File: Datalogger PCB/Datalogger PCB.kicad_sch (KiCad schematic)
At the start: 49 parts, among them J1 Conn_01x02_Pin, M1 Motor_Servo, M2 Motor_Servo, M3 Motor_Servo, M4 Motor_Servo, U1 Teensy4.1, U2 BNO055, U3 LPS25HB, U4 AMS1117-5.0, U5 ACPL-214-500E, U6 VN5E160STR-E, U7 VN5E160STR-E, U8 VN5E160STR-E, U9 VN5E160STR-E

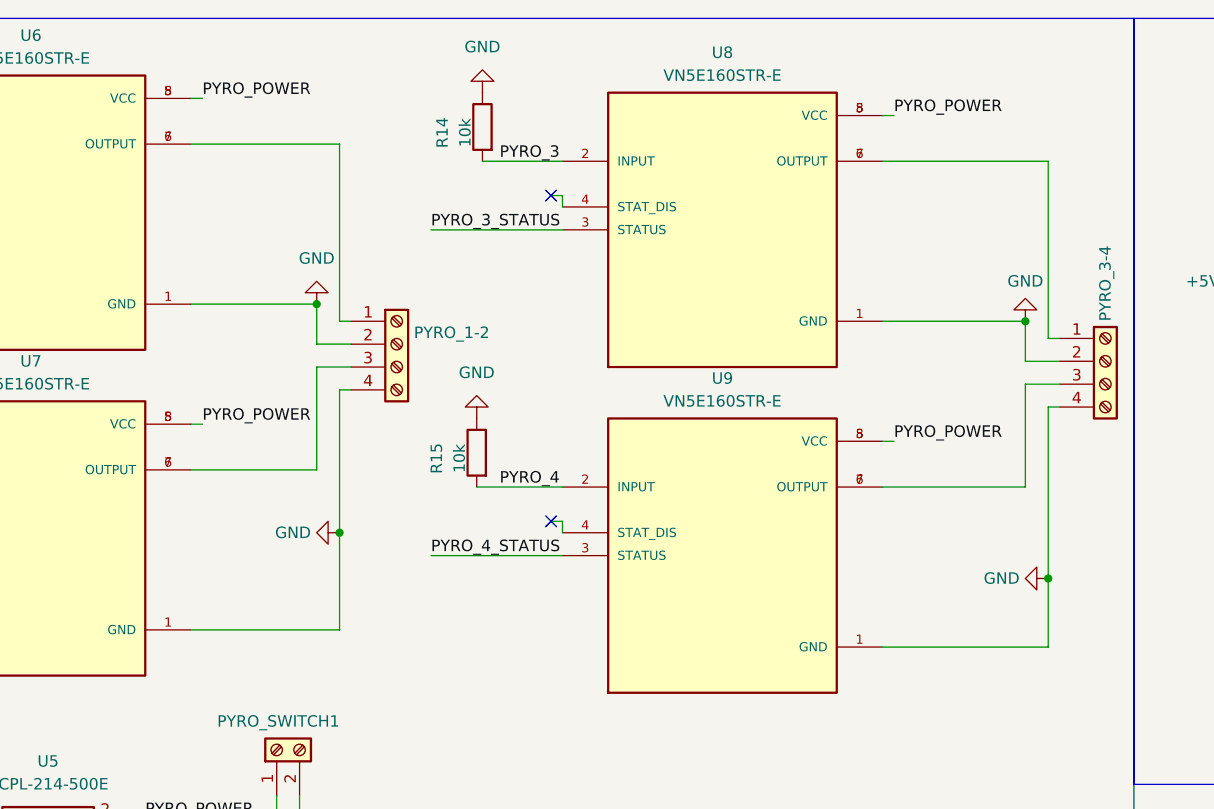
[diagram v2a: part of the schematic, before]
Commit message: Added continuity resistors
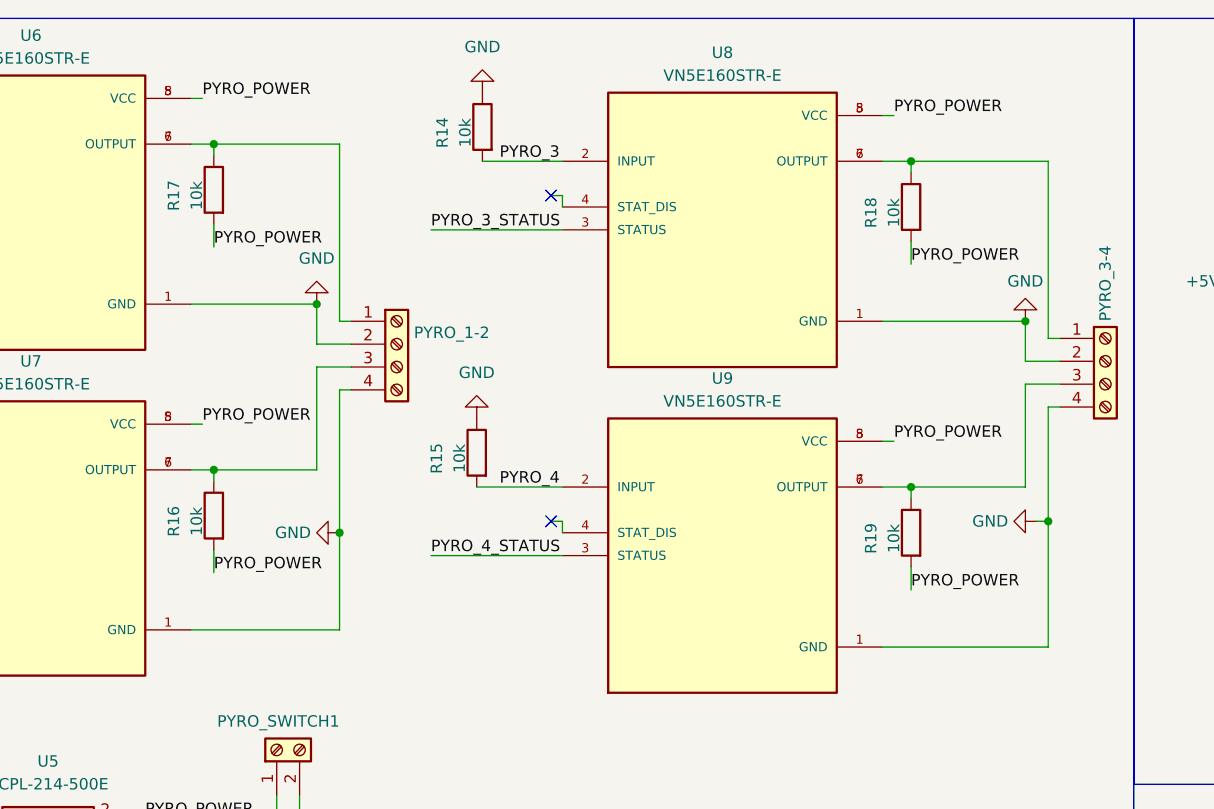
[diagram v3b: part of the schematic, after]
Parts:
- added R16, R17, R18, R19: 10k, Resistor_SMD:R_0603_1608Metric_Pad0.98x0.95mm_HandSolder, symbol Device:R
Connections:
- net PYRO_POWER: now also R16.2, R17.2, R18.2, R19.2
- net at PYRO_3-4.1 (Pin_1), U8.6 (OUTPUT), U8.7 (OUTPUT): now also R18.1
- net at PYRO_3-4.3 (Pin_3), U9.6 (OUTPUT), U9.7 (OUTPUT): now also R19.1
- net at PYRO_1-2.3 (Pin_3), U7.6 (OUTPUT), U7.7 (OUTPUT): now also R16.1
- net at PYRO_1-2.1 (Pin_1), U6.6 (OUTPUT), U6.7 (OUTPUT): now also R17.1

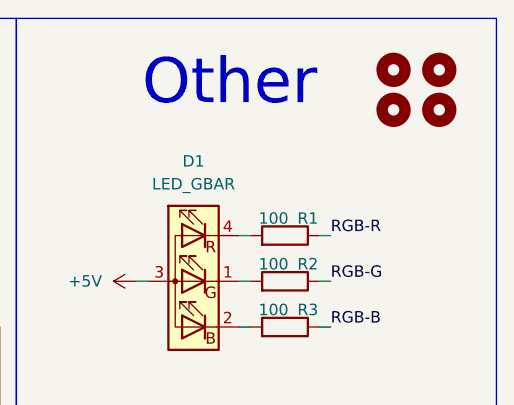
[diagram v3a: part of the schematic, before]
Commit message: Grounded Connector
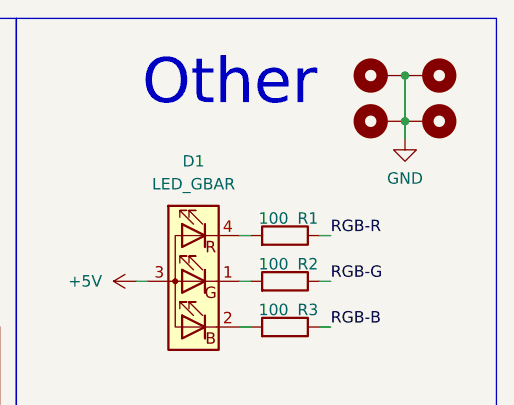
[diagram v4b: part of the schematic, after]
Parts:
- removed H1, H2, H3, H4: MountingHole, MountingHole:MountingHole_3.2mm_M3, symbol Mechanical:MountingHole
- added H1, H2, H3, H4: MountingHole_Pad, MountingHole:MountingHole_3.2mm_M3_Pad_TopBottom, symbol Mechanical:MountingHole_Pad
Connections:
- net GND: now also H1.1, H2.1, H3.1, H4.1
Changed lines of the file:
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@@
   (junction (at 214.63 193.04) (diameter 0) (color 0 0 0 0)
   )
+  (junction (at 333.375 23.495) (diameter 0) (color 0 0 0 0)
+  )
   (junction (at 114.935 155.575) (diameter 0) (color 0 0 0 0)
   )
+  (junction (at 333.375 18.415) (diameter 0) (color 0 0 0 0)
+  )
   (junction (at 280.67 67.945) (diameter 0) (color 0 0 0 0)
   )
@@
     (stroke (width 0) (type default))
   )
+  (wire (pts (xy 333.375 25.4) (xy 333.375 23.495))
+    (stroke (width 0) (type default))
+  )
   (wire (pts (xy 31.75 161.29) (xy 33.02 161.29))
     (stroke (width 0) (type default))
@@
     (stroke (width 0) (type default))
   )
+  (wire (pts (xy 333.375 18.415) (xy 333.375 23.495))
+    (stroke (width 0) (type default))
+  )
   (wire (pts (xy 199.39 164.465) (xy 198.12 164.465))
     (stroke (width 0) (type default))
@@
     (effects (font (size 1.27 1.27)) (justify left bottom))
   )
-  (symbol (lib_id "Mechanical:MountingHole") (at 337.185 22.225 0) (unit 1)
-    (in_bom no) (on_board yes) (dnp no) (fields_autoplaced)
-    (property "Reference" "H4" (at 339.725 20.955 0)
-      (effects (font (size 1.27 1.27)) (justify left) hide)
-    )
-    (property "Value" "MountingHole" (at 339.725 23.495 0)
-      (effects (font (size 1.27 1.27)) (justify left) hide)
-    )
-    (property "Footprint" "MountingHole:MountingHole_3.2mm_M3" (at 337.185 22.225 0)
-      (effects (font (size 1.27 1.27)) hide)
-    )
-    (property "Datasheet" "~" (at 337.185 22.225 0)
-      (effects (font (size 1.27 1.27)) hide)
-    )
-    (instances
-      (project "Datalogger PCB"
-        (path "/a3bc5533-d6ac-45b5-a7d9-fc1b12646794"
-          (reference "H4") (unit 1)
-        )
-      )
-    )
-  )
   (symbol (lib_id "power:GND") (at 182.88 195.58 270) (unit 1)
     (in_bom yes) (on_board yes) (dnp no) (fields_autoplaced)
@@
     )
   )
-  (symbol (lib_id "Mechanical:MountingHole") (at 332.105 17.78 0) (unit 1)
-    (in_bom no) (on_board yes) (dnp no) (fields_autoplaced)
-    (property "Reference" "H1" (at 334.645 16.51 0)
-      (effects (font (size 1.27 1.27)) (justify left) hide)
-    )
-    (property "Value" "MountingHole" (at 334.645 19.05 0)
-      (effects (font (size 1.27 1.27)) (justify left) hide)
-    )
-    (property "Footprint" "MountingHole:MountingHole_3.2mm_M3" (at 332.105 17.78 0)
-      (effects (font (size 1.27 1.27)) hide)
-    )
-    (property "Datasheet" "~" (at 332.105 17.78 0)
-      (effects (font (size 1.27 1.27)) hide)
-    )
-    (instances
-      (project "Datalogger PCB"
-        (path "/a3bc5533-d6ac-45b5-a7d9-fc1b12646794"
-          (reference "H1") (unit 1)
-        )
-      )
-    )
-  )
   (symbol (lib_id "power:+3.3V") (at 199.39 161.925 270) (unit 1)
     (in_bom yes) (on_board yes) (dnp no) (fields_autoplaced)
@@
     )
   )
+  (symbol (lib_id "Mechanical:MountingHole_Pad") (at 335.915 23.495 270) (unit 1)
+    (in_bom yes) (on_board yes) (dnp no)
+    (property "Reference" "H4" (at 338.455 26.67 0)
+      (effects (font (size 1.27 1.27)) (justify left) hide)
+    )
+    (property "Value" "MountingHole_Pad" (at 338.455 27.94 0)
+      (effects (font (size 1.27 1.27)) (justify left) hide)
+    )
+    (property "Footprint" "MountingHole:MountingHole_3.2mm_M3_Pad_TopBottom" (at 335.915 23.495 0)
+      (effects (font (size 1.27 1.27)) hide)
+    )
+    (property "Datasheet" "~" (at 335.915 23.495 0)
+      (effects (font (size 1.27 1.27)) hide)
+    )
+    (pin "1")
+    (instances
+      (project "Datalogger PCB"
+        (path "/a3bc5533-d6ac-45b5-a7d9-fc1b12646794"
+          (reference "H4") (unit 1)
+        )
+      )
+    )
+  )
   (symbol (lib_id "Device:LED_GBAR") (at 309.88 41.275 0) (mirror y) (unit 1)
     (in_bom yes) (on_board yes) (dnp no) (fields_autoplaced)
@@
     )
   )
+  (symbol (lib_id "power:GND") (at 333.375 25.4 0) (unit 1)
+    (in_bom yes) (on_board yes) (dnp no) (fields_autoplaced)
+    (property "Reference" "#PWR036" (at 333.375 31.75 0)
+      (effects (font (size 1.27 1.27)) hide)
+    )
+    (property "Value" "GND" (at 333.375 29.845 0)
+      (effects (font (size 1.27 1.27)))
+    )
+    (property "Footprint" "" (at 333.375 25.4 0)
+      (effects (font (size 1.27 1.27)) hide)
+    )
+    (property "Datasheet" "" (at 333.375 25.4 0)
+      (effects (font (size 1.27 1.27)) hide)
+    )
+    (pin "1")
+    (instances
+      (project "Datalogger PCB"
+        (path "/a3bc5533-d6ac-45b5-a7d9-fc1b12646794"
+          (reference "#PWR036") (unit 1)
+        )
+      )
+    )
+  )
   (symbol (lib_id "Device:C") (at 109.855 158.75 270) (mirror x) (unit 1)
     (in_bom yes) (on_board yes) (dnp no)
@@
     )
   )
+  (symbol (lib_id "Mechanical:MountingHole_Pad") (at 330.835 18.415 90) (unit 1)
+    (in_bom yes) (on_board yes) (dnp no)
+    (property "Reference" "H1" (at 328.295 15.24 0)
+      (effects (font (size 1.27 1.27)) (justify left) hide)
+    )
+    (property "Value" "MountingHole_Pad" (at 328.295 13.97 0)
+      (effects (font (size 1.27 1.27)) (justify left) hide)
+    )
+    (property "Footprint" "MountingHole:MountingHole_3.2mm_M3_Pad_TopBottom" (at 330.835 18.415 0)
+      (effects (font (size 1.27 1.27)) hide)
+    )
+    (property "Datasheet" "~" (at 330.835 18.415 0)
+      (effects (font (size 1.27 1.27)) hide)
+    )
+    (pin "1")
+    (instances
+      (project "Datalogger PCB"
+        (path "/a3bc5533-d6ac-45b5-a7d9-fc1b12646794"
+          (reference "H1") (unit 1)
+        )
+      )
+    )
+  )
   (symbol (lib_id "power:GND") (at 308.61 63.5 270) (mirror x) (unit 1)
     (in_bom yes) (on_board yes) (dnp no) (fields_autoplaced)
@@
     )
   )
-  (symbol (lib_id "Mechanical:MountingHole") (at 332.105 22.225 0) (unit 1)
-    (in_bom no) (on_board yes) (dnp no) (fields_autoplaced)
-    (property "Reference" "H3" (at 334.645 20.955 0)
-      (effects (font (size 1.27 1.27)) (justify left) hide)
-    )
-    (property "Value" "MountingHole" (at 334.645 23.495 0)
-      (effects (font (size 1.27 1.27)) (justify left) hide)
-    )
-    (property "Footprint" "MountingHole:MountingHole_3.2mm_M3" (at 332.105 22.225 0)
-      (effects (font (size 1.27 1.27)) hide)
-    )
-    (property "Datasheet" "~" (at 332.105 22.225 0)
-      (effects (font (size 1.27 1.27)) hide)
-    )
-    (instances
-      (project "Datalogger PCB"
-        (path "/a3bc5533-d6ac-45b5-a7d9-fc1b12646794"
-          (reference "H3") (unit 1)
-        )
-      )
-    )
-  )
   (symbol (lib_id "power:+5V") (at 308.61 87.63 90) (unit 1)
     (in_bom yes) (on_board yes) (dnp no) (fields_autoplaced)
@@
     )
   )
+  (symbol (lib_id "Mechanical:MountingHole_Pad") (at 335.915 18.415 270) (unit 1)
+    (in_bom yes) (on_board yes) (dnp no)
+    (property "Reference" "H2" (at 338.455 21.59 0)
+      (effects (font (size 1.27 1.27)) (justify left) hide)
+    )
+    (property "Value" "MountingHole_Pad" (at 338.455 22.86 0)
+      (effects (font (size 1.27 1.27)) (justify left) hide)
+    )
+    (property "Footprint" "MountingHole:MountingHole_3.2mm_M3_Pad_TopBottom" (at 335.915 18.415 0)
+      (effects (font (size 1.27 1.27)) hide)
+    )
+    (property "Datasheet" "~" (at 335.915 18.415 0)
+      (effects (font (size 1.27 1.27)) hide)
+    )
+    (pin "1")
+    (instances
+      (project "Datalogger PCB"
+        (path "/a3bc5533-d6ac-45b5-a7d9-fc1b12646794"
+          (reference "H2") (unit 1)
+        )
+      )
+    )
+  )
   (symbol (lib_id "Device:C") (at 223.52 188.595 0) (mirror x) (unit 1)
     (in_bom yes) (on_board yes) (dnp no)
@@
     )
   )
+  (symbol (lib_id "Mechanical:MountingHole_Pad") (at 330.835 23.495 90) (unit 1)
+    (in_bom yes) (on_board yes) (dnp no)
+    (property "Reference" "H3" (at 328.295 20.32 0)
+      (effects (font (size 1.27 1.27)) (justify left) hide)
+    )
+    (property "Value" "MountingHole_Pad" (at 328.295 19.05 0)
+      (effects (font (size 1.27 1.27)) (justify left) hide)
+    )
+    (property "Footprint" "MountingHole:MountingHole_3.2mm_M3_Pad_TopBottom" (at 330.835 23.495 0)
+      (effects (font (size 1.27 1.27)) hide)
+    )
+    (property "Datasheet" "~" (at 330.835 23.495 0)
+      (effects (font (size 1.27 1.27)) hide)
+    )
+    (pin "1")
+    (instances
+      (project "Datalogger PCB"
+        (path "/a3bc5533-d6ac-45b5-a7d9-fc1b12646794"
+          (reference "H3") (unit 1)
+        )
+      )
+    )
+  )
   (symbol (lib_id "Sensor_Motion:BNO055") (at 48.26 173.99 0) (unit 1)
     (in_bom yes) (on_board yes) (dnp no) (fields_autoplaced)
@@
         )
       )
-    )
-  )
-  (symbol (lib_id "Mechanical:MountingHole") (at 337.185 17.78 0) (unit 1)
-    (in_bom no) (on_board yes) (dnp no) (fields_autoplaced)
-    (property "Reference" "H2" (at 339.725 16.51 0)
-      (effects (font (size 1.27 1.27)) (justify left) hide)
-    )
-    (property "Value" "MountingHole" (at 339.725 19.05 0)
-      (effects (font (size 1.27 1.27)) (justify left) hide)
-    )
-    (property "Footprint" "MountingHole:MountingHole_3.2mm_M3" (at 337.185 17.78 0)
-      (effects (font (size 1.27 1.27)) hide)
-    )
-    (property "Datasheet" "~" (at 337.185 17.78 0)
-      (effects (font (size 1.27 1.27)) hide)
-    )
-    (instances
-      (project "Datalogger PCB"
-        (path "/a3bc5533-d6ac-45b5-a7d9-fc1b12646794"
-          (reference "H2") (unit 1)
-        )
-      )

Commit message: Made power jumper standard
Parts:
- JP1: footprint Connector_PinHeader_2.00mm:PinHeader_1x02_P2.00mm_Vertical -> Connector_PinHeader_2.54mm:PinHeader_1x02_P2.54mm_Vertical
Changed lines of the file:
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@@
       (effects (font (size 1.27 1.27)) (justify right))
     )
-    (property "Footprint" "Connector_PinHeader_2.00mm:PinHeader_1x02_P2.00mm_Vertical" (at 224.79 179.705 0)
+    (property "Footprint" "Connector_PinHeader_2.54mm:PinHeader_1x02_P2.54mm_Vertical" (at 224.79 179.705 0)
       (effects (font (size 1.27 1.27)) hide)
     )
